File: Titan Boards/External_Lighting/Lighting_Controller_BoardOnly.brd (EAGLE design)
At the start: 44.8 x 21.5 mm, 24 parts, among them J1 SOLDER2PAD, J10 SOLDER2PAD, J11 SOLDER3PAD, J12 SOLDER3PAD, J13 SOLDER2PAD, J14 SOLDER2PAD, J15 SOLDER3PAD, J16 SOLDER3PAD, J2 SOLDER2PAD, J3 SOLDER3PAD, J4 SOLDER3PAD, J5 SOLDER2PAD, J6 SOLDER2PAD, J7 SOLDER3PAD, J8 SOLDER3PAD, J9 SOLDER2PAD

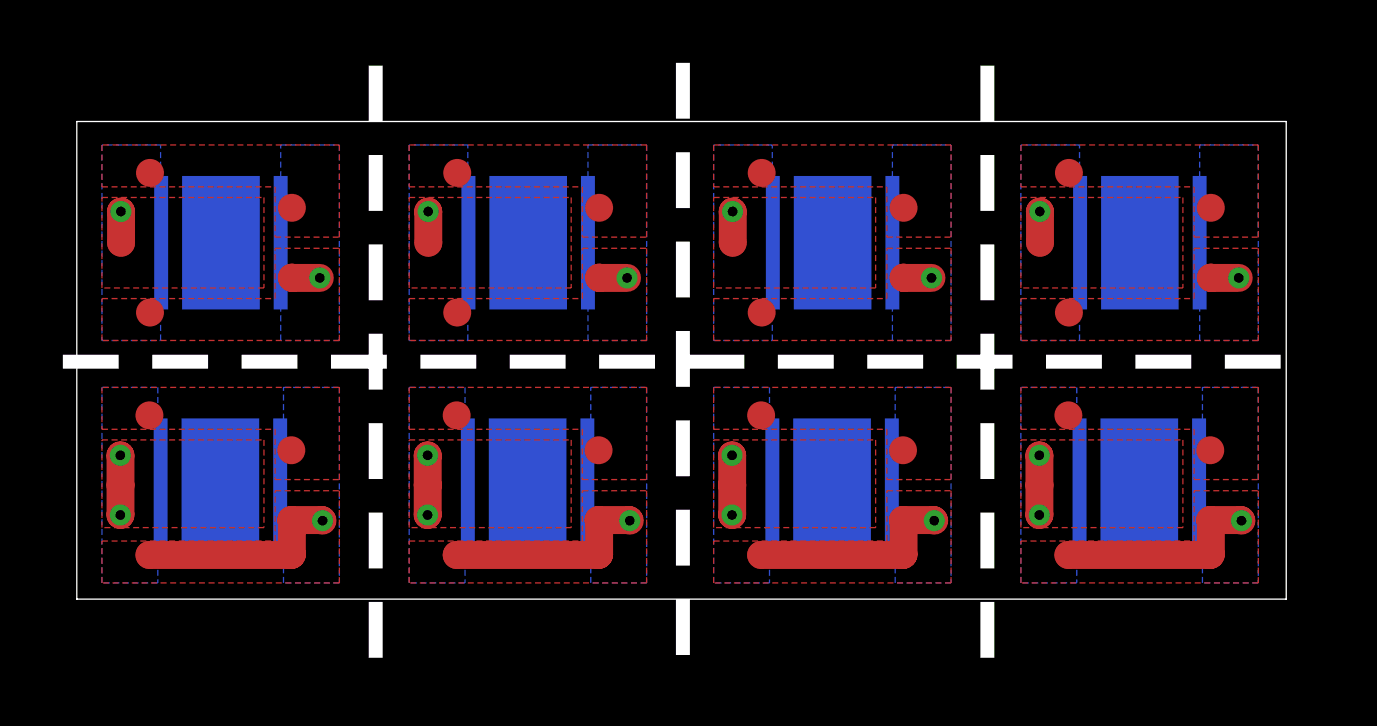
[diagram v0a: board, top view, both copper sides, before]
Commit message: Fixed Panelization
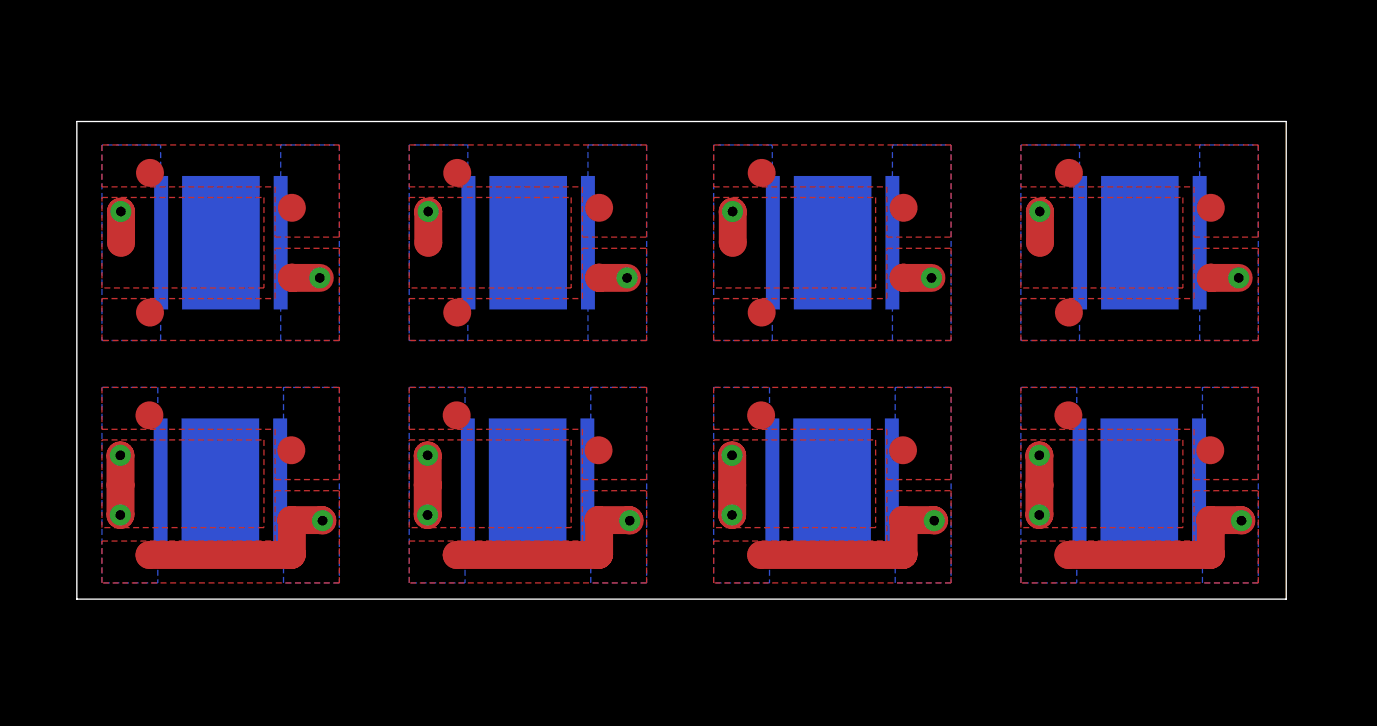
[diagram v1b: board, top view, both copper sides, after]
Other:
- board size 44.8 x 21.5 mm -> 43.3 x 17.1 mm
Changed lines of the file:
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@@
 <text x="1.750009375" y="12.5499875" size="1.27" layer="126" rot="MR180">D9</text>
 <text x="1.750009375" y="2.110003125" size="1.27" layer="126" rot="MR180">D10</text>
-<wire x1="10.7" y1="19.1" x2="10.7" y2="-2.3" width="0.5" layer="20" style="shortdash"/>
-<wire x1="21.7" y1="19.2" x2="21.7" y2="-2.2" width="0.5" layer="20" style="shortdash"/>
-<wire x1="32.6" y1="19.1" x2="32.6" y2="-2.3" width="0.5" layer="20" style="shortdash"/>
+<wire x1="10.7" y1="19.1" x2="10.7" y2="-2.3" width="0.5" layer="45" style="shortdash"/>
+<wire x1="21.7" y1="19.2" x2="21.7" y2="-2.2" width="0.5" layer="45" style="shortdash"/>
+<wire x1="32.6" y1="19.1" x2="32.6" y2="-2.3" width="0.5" layer="45" style="shortdash"/>
 <wire x1="0" y1="0" x2="43.3" y2="0" width="0" layer="20"/>
 <wire x1="43.3" y1="0" x2="43.3" y2="17.1" width="0" layer="20"/>
 <wire x1="43.3" y1="17.1" x2="0" y2="17.1" width="0" layer="20"/>
 <wire x1="0" y1="17.1" x2="0" y2="0" width="0" layer="20"/>
-<wire x1="-0.5" y1="8.5" x2="44.3" y2="8.5" width="0.5" layer="20" style="shortdash"/>
+<wire x1="-0.5" y1="8.5" x2="44.3" y2="8.5" width="0.5" layer="45" style="shortdash"/>
 </plain>
 <attributes>

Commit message: Larger Soldering Pads
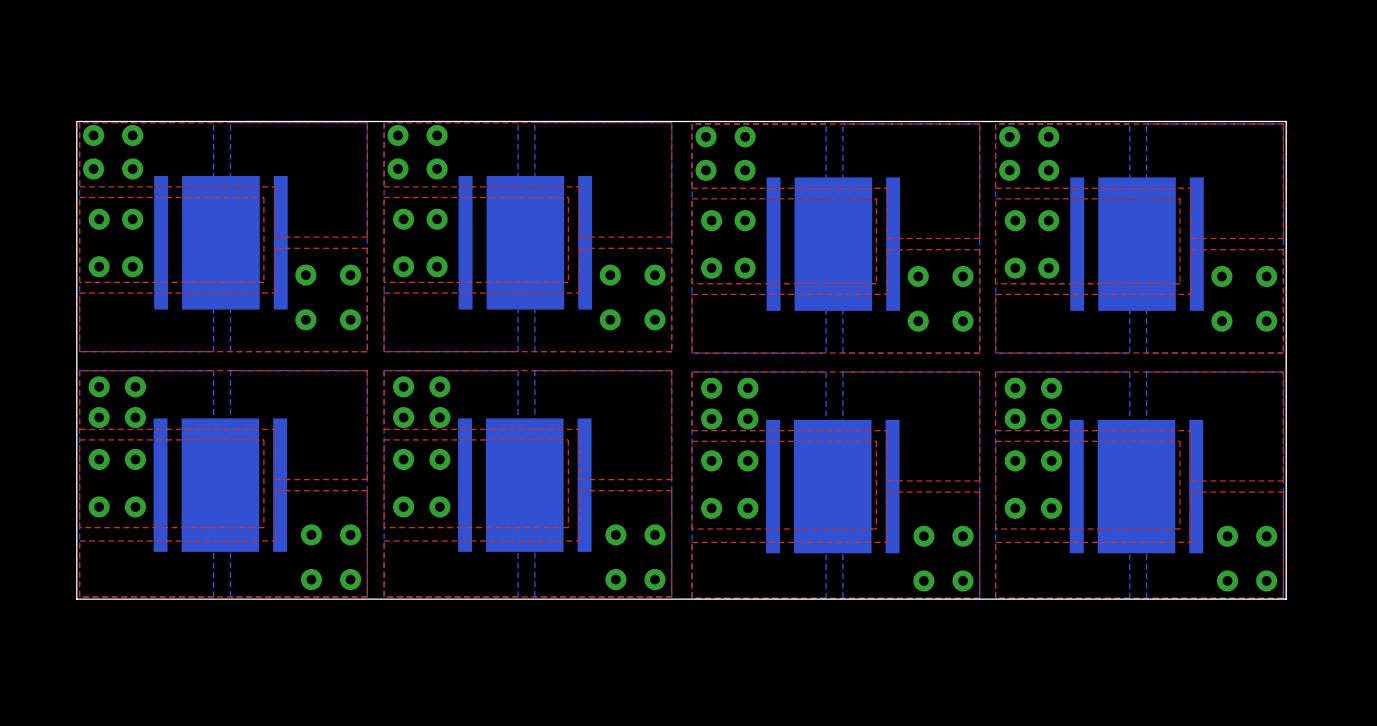
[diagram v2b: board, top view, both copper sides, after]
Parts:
- removed J1, J10, J13, J14, J2, J5, J6, J9: SOLDER2PAD, Molex_0436500302:SOLDER2PAD
- removed J11, J12, J15, J16, J3, J4, J7, J8: SOLDER3PAD, Molex_0436500302:SOLDER3PAD
- moved D6 0.11 mm to (38.0, 12.7)
- moved D5 0.11 mm to (37.9, 4.03)
- moved D1 0.10 mm to (16.0, 4.08)
- moved D2 0.10 mm to (16.1, 12.8)
- moved D3 0.06 mm to (27.1, 4.03)
- moved D4 0.06 mm to (27.1, 12.7)
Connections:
- removed net N$15: D9.2, J3.P$2
- removed net N$4: D4.2, J11.P$2
- removed net N$5: D5.1, J16.P$2
- removed net N$6: D6.2, J15.P$2
- net 12V: no longer J1.P$2, J2.P$1, J3.P$3, J4.P$1
- net 12V1: no longer J5.P$2, J6.P$1, J7.P$3, J8.P$1
- net 12V2: no longer J10.P$1, J11.P$3, J12.P$1, J9.P$2
- net 12V3: no longer J13.P$2, J14.P$1, J15.P$3, J16.P$1
- net GND: no longer J1.P$1, J2.P$2, J3.P$1, J4.P$3
- net GND1: no longer J5.P$1, J6.P$2, J7.P$1, J8.P$3
- net GND2: no longer J10.P$2, J11.P$1, J12.P$3, J9.P$1
- net GND3: no longer J13.P$1, J14.P$2, J15.P$1, J16.P$3
- net N$1: now also D2.2; no longer J8.P$2
- net N$12: now also D9.2; no longer J4.P$2
- net N$2: now also D3.1, D4.2; no longer D2.2, J7.P$2
- net N$3: now also D5.1, D6.2; no longer D3.1, J12.P$2
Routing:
- net GND2: track 7.47 -> 0.00 mm, vias 1 -> 8
- net GND3: track 7.47 -> 0.00 mm, vias 1 -> 8
- net GND: track 7.47 -> 0.00 mm, vias 1 -> 8
- net GND1: track 7.47 -> 0.00 mm, vias 1 -> 8
- net N$5: track 2.14 -> 0.00 mm, vias 2 -> 0
- net N$12: track 2.14 -> 0.00 mm, vias 2 -> 8
- net N$1: track 2.14 -> 0.00 mm, vias 2 -> 8
- net N$3: track 2.14 -> 0.00 mm, vias 2 -> 8
- net N$6: track 1.12 -> 0.00 mm, vias 1 -> 0
- net N$4: track 1.12 -> 0.00 mm, vias 1 -> 0
- net N$15: track 1.12 -> 0.00 mm, vias 1 -> 0
- net N$2: track 1.12 -> 0.00 mm, vias 1 -> 8
- net 12V3: track 1.00 -> 0.00 mm, vias 1 -> 8
- net 12V2: track 1.00 -> 0.00 mm, vias 1 -> 8
- net 12V1: track 1.00 -> 0.00 mm, vias 1 -> 8
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- added copper zone on layer 1, net N$1
- added copper zone on layer 1, net N$12
- added copper zone on layer 1, net N$2
- added copper zone on layer 16, net N$2
- added copper zone on layer 1, net N$3
- removed copper zone on layer 16, net N$5
- removed copper zone on layer 1, net P$1
- removed copper zone on layer 16, net P$1
- removed copper zone on layer 1, net P$2
- removed copper zone on layer 16, net P$2
- removed copper zone on layer 1, net P$3
- removed copper zone on layer 16, net P$3
- removed copper zone on layer 1, net P$4
- removed copper zone on layer 16, net P$4

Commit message: Perferated external lighting board and removed top right set of vias
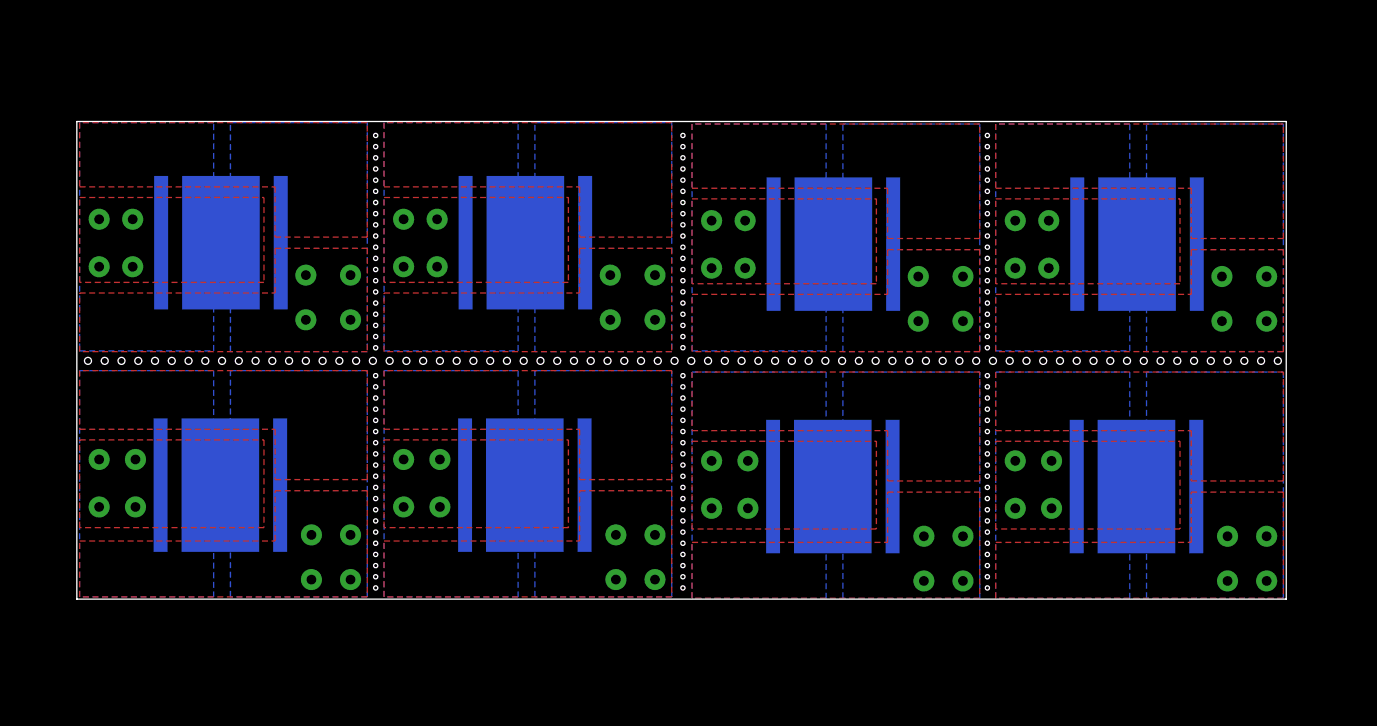
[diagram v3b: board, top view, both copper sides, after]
